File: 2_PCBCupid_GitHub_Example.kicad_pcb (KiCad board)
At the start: 2 copper layers, 1 part

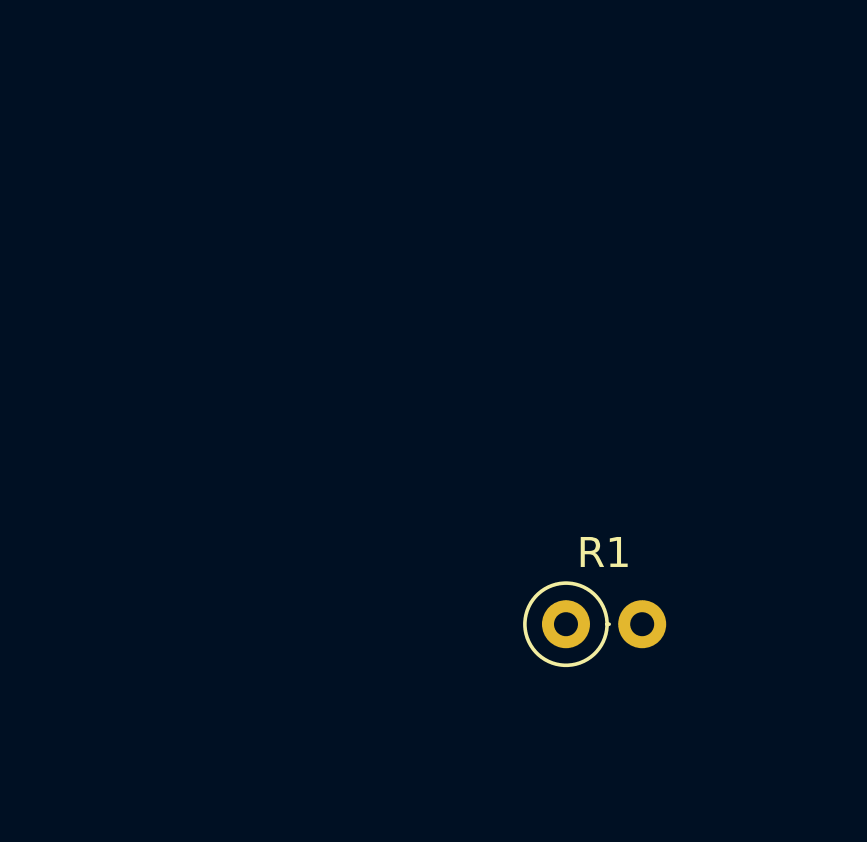
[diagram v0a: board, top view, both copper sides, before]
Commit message: Fixed swithc 2 schematic and pcb layout
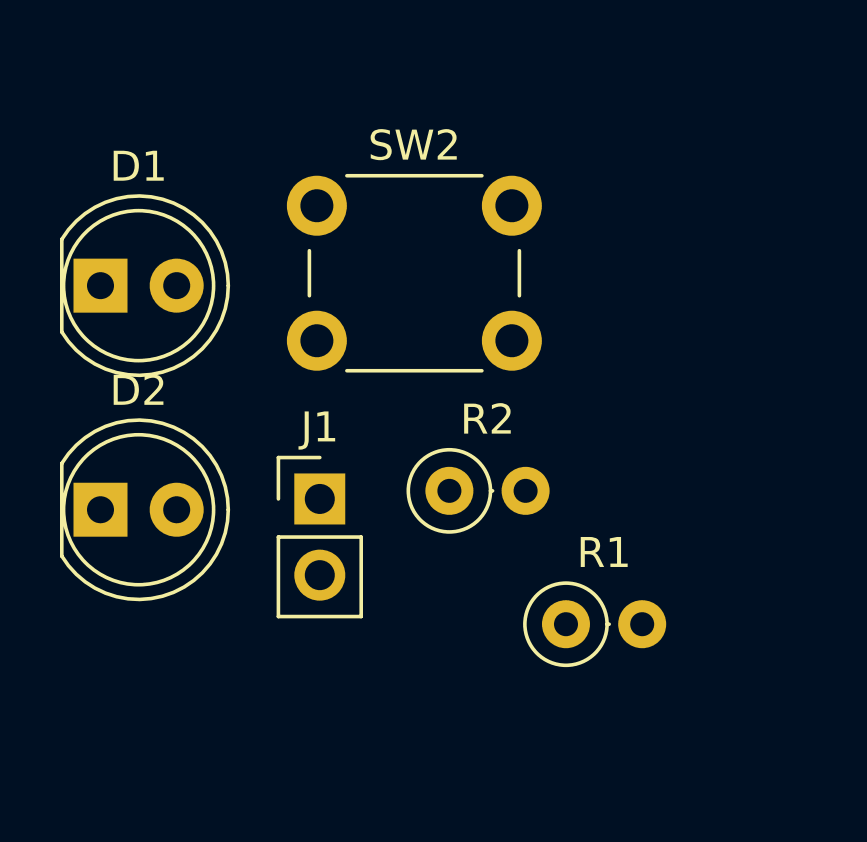
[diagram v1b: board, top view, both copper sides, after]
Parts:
- added D1: LED, LED_THT:LED_D5.0mm, F.Cu at (122.6, 84.8)
- added D2: LED, LED_THT:LED_D5.0mm, F.Cu at (122.6, 92.3)
- added J1: Conn_01x02, Connector_PinHeader_2.54mm:PinHeader_1x02_P2.54mm_Vertical, F.Cu at (129.9, 91.9)
- added R2: R, Resistor_THT:R_Axial_DIN0207_L6.3mm_D2.5mm_P2.54mm_Vertical, F.Cu at (134.2, 91.6)
- added SW2: SW_DPST_x2, Button_Switch_THT:SW_PUSH_6mm, F.Cu at (129.8, 82.1)

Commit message: Layout completed
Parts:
- moved D2 14.7 mm to (137.1, 90.1), turned to -90 degrees
- moved J1 14.0 mm to (142.8, 86.6)
- moved D1 9.41 mm to (130.3, 90.1), turned to -90 degrees
- moved R1 8.79 mm to (129.3, 96.7)
- moved SW2 8.13 mm to (137.0, 85.8), turned to 180 degrees
- moved R2 6.44 mm to (138.2, 96.7), turned to 180 degrees
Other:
- board outline added: 24 x 24 mm

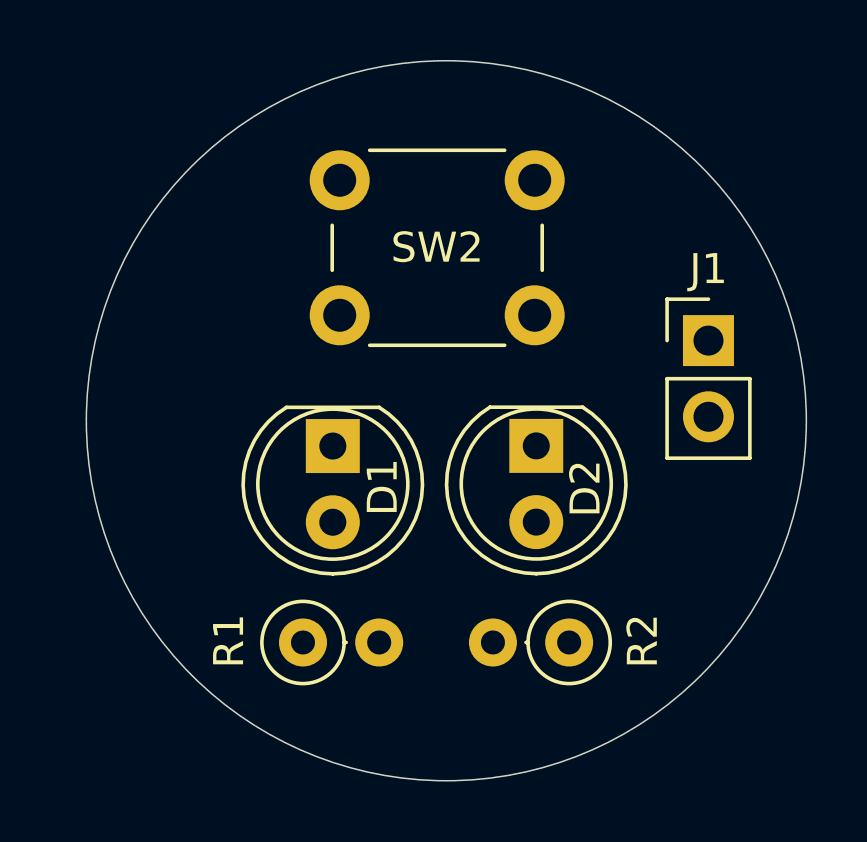
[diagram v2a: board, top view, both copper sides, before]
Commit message: SMD schematic and layout completed
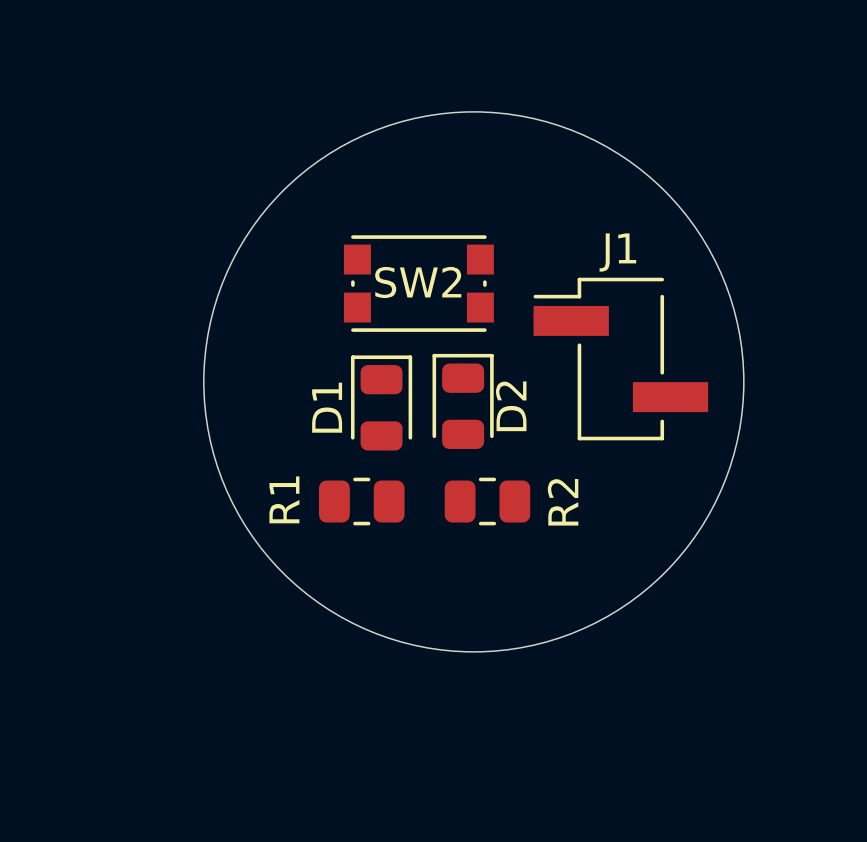
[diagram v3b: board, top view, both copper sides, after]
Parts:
- D1, D2: footprint LED_THT:LED_D5.0mm -> LED_SMD:LED_0805_2012Metric
- J1: footprint Connector_PinHeader_2.54mm:PinHeader_1x02_P2.54mm_Vertical -> Connector_PinHeader_2.54mm:PinHeader_1x02_P2.54mm_Vertical_SMD_Pin1Left
- R1, R2: footprint Resistor_THT:R_Axial_DIN0207_L6.3mm_D2.5mm_P2.54mm_Vertical -> Resistor_SMD:R_0805_2012Metric
- SW2: footprint Button_Switch_THT:SW_PUSH_6mm -> Button_Switch_SMD:SW_Push_1P1T_NO_CK_KMR2
- moved R2 5.43 mm to (135.5, 92.0), turned to 0 degrees
- moved R1 5.09 mm to (131.3, 92.0)
- moved SW2 4.00 mm to (133.2, 84.7)
- moved J1 2.98 mm to (139.9, 87.2)
- moved D2 2.77 mm to (134.6, 88.8)
- moved D1 2.07 mm to (131.9, 88.9)
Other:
- board size 24 x 24 mm -> 18 x 18 mm

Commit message: Routing completed
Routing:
- net Net-(D1-K): track 0.00 -> 9.43 mm
- net VCC: track 0.00 -> 8.72 mm
- net Net-(D1-A): track 0.00 -> 3.36 mm
- net GND: track 0.00 -> 3.20 mm, vias 0 -> 3
- net Net-(D2-A): track 0.00 -> 2.28 mm
- added copper zone on B.Cu, net GND
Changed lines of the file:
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@@
 		(tags "Surface mounted pin header SMD 1x02 2.54mm single row style1 pin1 left")
 		(property "Reference" "J1"
-			(at 0 -3.65 0)
+			(at -2.2352 0.2794 0)
 			(layer "F.SilkS")
 			(effects
@@
 		(tags "LED")
 		(property "Reference" "D2"
-			(at 0 -1.65 270)
+			(at 0.4826 -1.778 270)
 			(layer "F.SilkS")
 			(effects
@@
 		(layer "Edge.Cuts")
 	)
+	(segment
+		(start 130.3547 90.4983)
+		(end 130.3547 91.9988)
+		(width 0.2)
+		(layer "F.Cu")
+		(net 1)
+	)
+	(segment
+		(start 131.9276 89.8121)
+		(end 131.0409 89.8121)
+		(width 0.2)
+		(layer "F.Cu")
+		(net 1)
+	)
+	(segment
+		(start 131.0409 89.8121)
+		(end 130.3547 90.4983)
+		(width 0.2)
+		(layer "F.Cu")
+		(net 1)
+	)
+	(segment
+		(start 131.3688 91.9988)
+		(end 132.1797 91.9988)
+		(width 0.2)
+		(layer "F.Cu")
+		(net 2)
+	)
+	(segment
+		(start 135.5598 91.9988)
+		(end 136.3707 91.9988)
+		(width 0.2)
+		(layer "F.Cu")
+		(net 2)
+	)
+	(segment
+		(start 139.9794 88.519)
+		(end 141.5582 88.519)
+		(width 0.2)
+		(layer "F.Cu")
+		(net 2)
+	)
+	(via
+		(at 139.9794 88.519)
+		(size 0.6)
+		(drill 0.3)
+		(layers "F.Cu" "B.Cu")
+		(free yes)
+		(net 2)
+	)
+	(via
+		(at 131.3688 91.9988)
+		(size 0.6)
+		(drill 0.3)
+		(layers "F.Cu" "B.Cu")
+		(free yes)
+		(net 2)
+	)
+	(via
+		(at 135.5598 91.9988)
+		(size 0.6)
+		(drill 0.3)
+		(layers "F.Cu" "B.Cu")
+		(free yes)
+		(net 2)
+	)
+	(segment
+		(start 131.1222 85.5344)
+		(end 131.1222 87.1317)
+		(width 0.2)
+		(layer "F.Cu")
+		(net 3)
+	)
+	(segment
+		(start 131.1222 87.1317)
+		(end 131.9276 87.9371)
+		(width 0.2)
+		(layer "F.Cu")
+		(net 3)
+	)
+	(segment
+		(start 135.2222 85.5344)
+		(end 135.2222 87.3095)
+		(width 0.2)
+		(layer "F.Cu")
+		(net 3)
+	)
+	(segment
+		(start 135.2222 87.3095)
+		(end 134.6454 87.8863)
+		(width 0.2)
+		(layer "F.Cu")
+		(net 3)
+	)
+	(segment
+		(start 135.2222 85.5344)
+		(end 131.1222 85.5344)
+		(width 0.2)
+		(layer "F.Cu")
+		(net 3)
+	)
+	(segment
+		(start 134.6454 91.8991)
+		(end 134.5457 91.9988)
+		(width 0.2)
+		(layer "F.Cu")
+		(net 4)
+	)
+	(segment
+		(start 134.6454 89.7613)
+		(end 134.6454 91.8991)
+		(width 0.2)
+		(layer "F.Cu")
+		(net 4)
+	)
+	(segment
+		(start 131.1222 83.9344)
+		(end 135.2222 83.9344)
+		(width 0.2)
+		(layer "F.Cu")
+		(net 5)
+	)
+	(segment
+		(start 138.2482 84.705)
+		(end 137.4776 83.9344)
+		(width 0.2)
+		(layer "F.Cu")
+		(net 5)
+	)
+	(segment
+		(start 137.4776 83.9344)
+		(end 135.2222 83.9344)
+		(width 0.2)
+		(layer "F.Cu")
+		(net 5)
+	)
+	(segment
+		(start 138.2482 85.979)
+		(end 138.2482 84.705)
+		(width 0.2)
+		(layer "F.Cu")
+		(net 5)
+	)
+	(zone
+		(net 2)
+		(net_name "GND")
+		(layer "B.Cu")
+		(hatch edge 0.5)
+		(connect_pads
+			(clearance 0.5)
+		)
+		(min_thickness 0.25)
+		(filled_areas_thickness no)
+		(fill yes
+			(thermal_gap 0.5)
+			(thermal_bridge_width 0.5)
+		)
+		(polygon
+			(pts
+				(xy 125.830414 78.8924) (xy 144.599289 78.8924) (xy 144.556334 97.363034) (xy 125.615562 97.326817)
+			)
+		)
+	)
 	(embedded_fonts no)
